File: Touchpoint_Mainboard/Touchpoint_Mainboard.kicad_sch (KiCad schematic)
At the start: 31 parts, among them J2 Conn_01x02, U4 NCP1117-3.3_SOT223, U5 W25Q128JVS, U6 RP2040, Y1 ABM8-272-T3

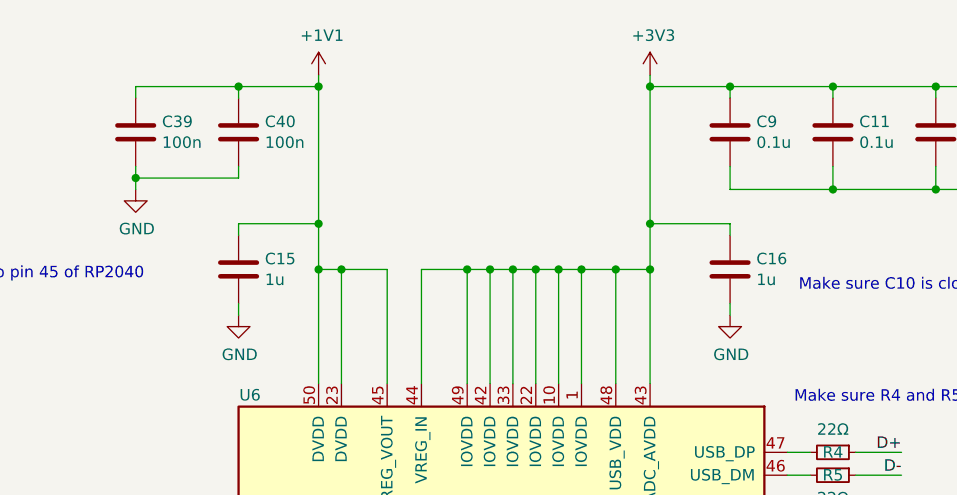
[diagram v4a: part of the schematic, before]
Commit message: Finished assigning footprints and 3d models for both boards
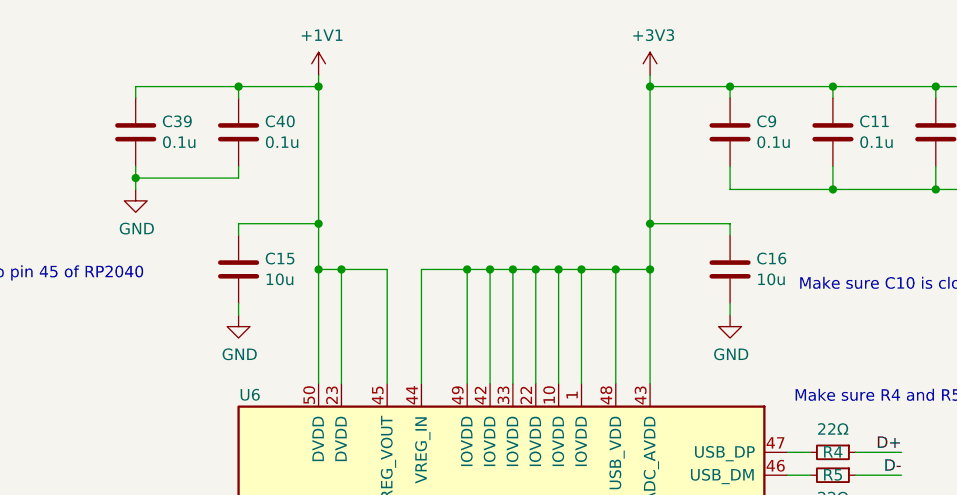
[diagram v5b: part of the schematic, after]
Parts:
- C15, C16: value 1u -> 10u
- C39, C40: value 100n -> 0.1u
- U5: footprint Package_SO:SOIC-8_5.23x5.23mm_P1.27mm -> Package_SO:SOIC-8_5.3x5.3mm_P1.27mm
- U6: footprint RP2040_minimal:RP2040-QFN-56 -> Package_DFN_QFN:QFN-56-1EP_7x7mm_P0.4mm_EP3.2x3.2mm
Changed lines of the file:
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@@
 			)
 		)
-		(property "Value" "1u"
+		(property "Value" "10u"
 			(at 38.481 45.593 0)
 			(effects
@@
 			)
 		)
-		(property "Value" "1u"
+		(property "Value" "10u"
 			(at 93.091 45.593 0)
 			(effects
@@
 			)
 		)
-		(property "Footprint" "Package_SO:SOIC-8_5.23x5.23mm_P1.27mm"
+		(property "Footprint" "Package_SO:SOIC-8_5.3x5.3mm_P1.27mm"
 			(at 229.87 121.92 0)
 			(effects
@@
 			)
 		)
-		(property "Footprint" "RP2040_minimal:RP2040-QFN-56"
+		(property "Footprint" "Package_DFN_QFN:QFN-56-1EP_7x7mm_P0.4mm_EP3.2x3.2mm"
 			(at 45.72 107.95 0)
 			(effects
@@
 			)
 		)
-		(property "Value" "100n"
+		(property "Value" "0.1u"
 			(at 38.481 30.353 0)
 			(effects
@@
 			)
 		)
-		(property "Value" "100n"
+		(property "Value" "0.1u"
 			(at 27.051 30.353 0)
 			(effects

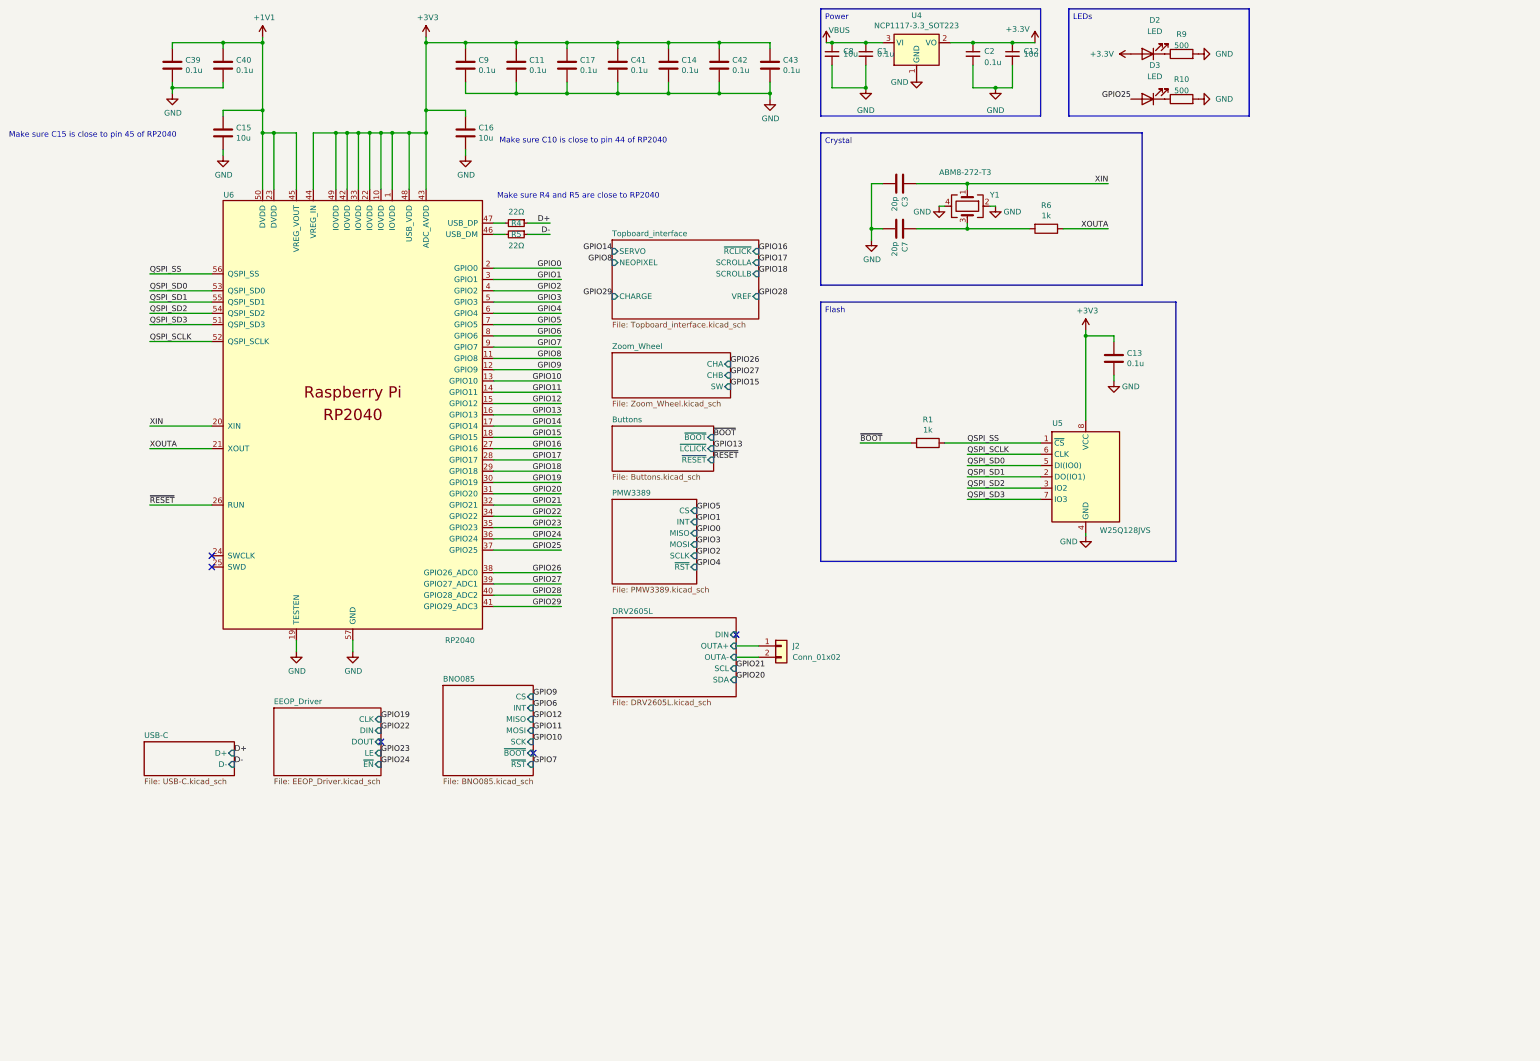
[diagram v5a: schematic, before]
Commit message: Added 3.3V to interface
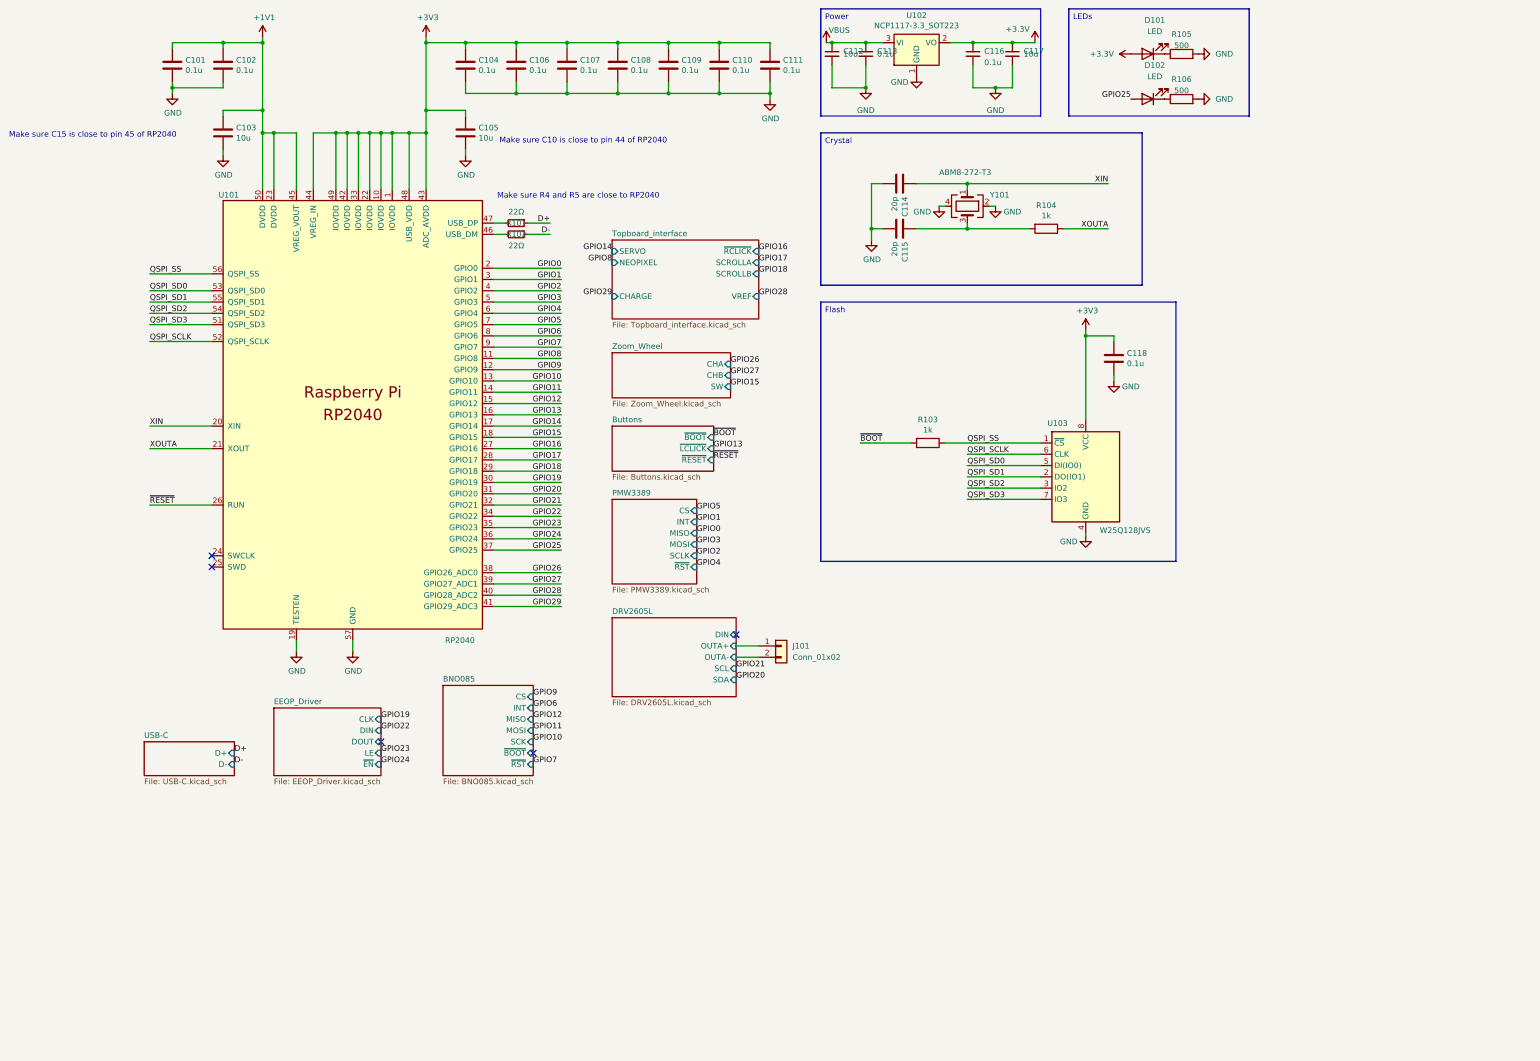
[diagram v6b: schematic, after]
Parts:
- renumbered C39 to C101, C40 to C102, C15 to C103, C9 to C104, C16 to C105, C11 to C106, C17 to C107, C41 to C108, C14 to C109, C42 to C110, C43 to C111, C8 to C112, C1 to C113, C3 to C114, C7 to C115, C2 to C116, C12 to C117, C13 to C118, D2 to D101, D3 to D102, J2 to J101, R4 to R101, R5 to R102, R1 to R103, R6 to R104, R9 to R105, R10 to R106, U6 to U101, U4 to U102, U5 to U103, Y1 to Y101

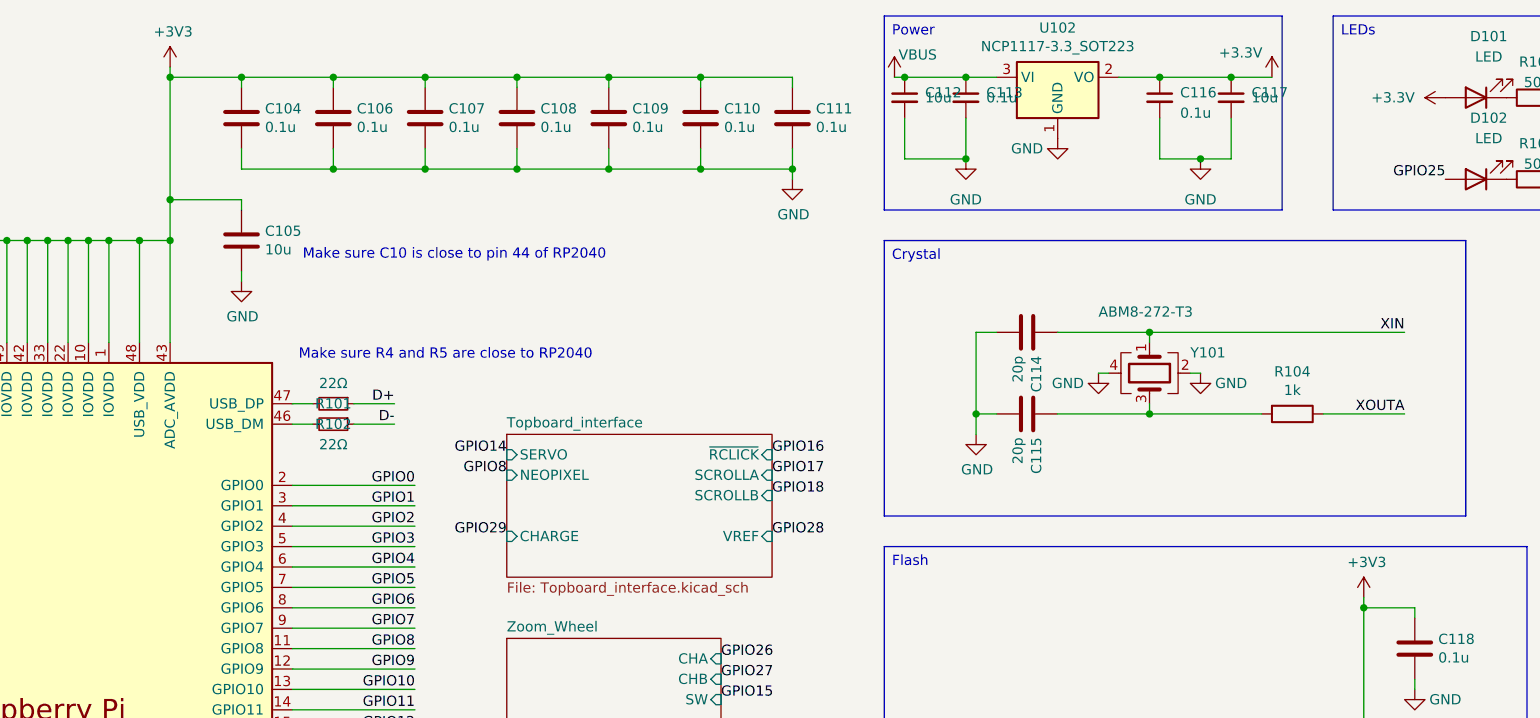
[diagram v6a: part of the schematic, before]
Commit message: Working through mainboard routing
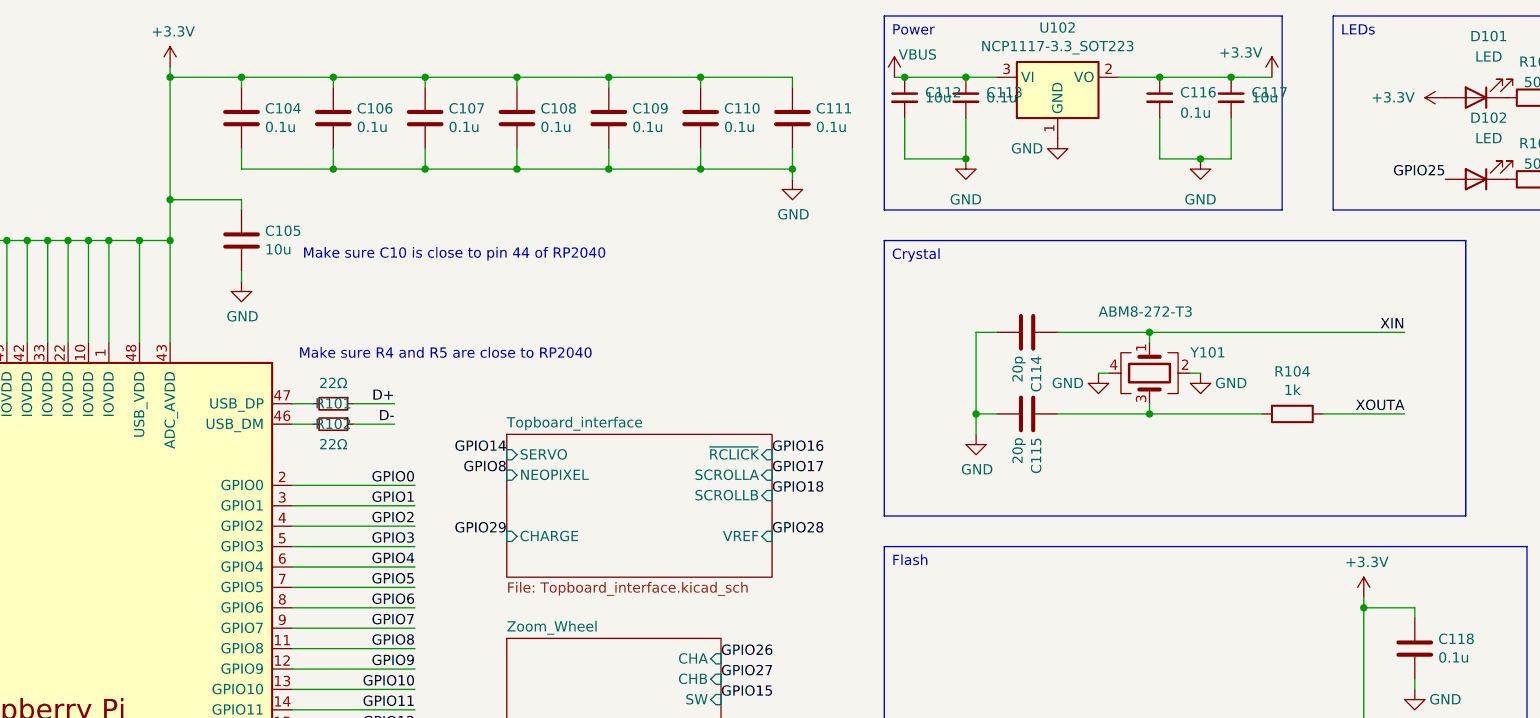
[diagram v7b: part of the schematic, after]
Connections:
- net +3V3 is gone; now on net +3.3V: C104.1, C105.1, C106.1, C107.1, C108.1, C109.1, C110.1, C111.1, C118.1, U101.1 (IOVDD), U101.10 (IOVDD), U101.22 (IOVDD), U101.33 (IOVDD), U101.42 (IOVDD), U101.43 (ADC_AVDD), U101.44 (VREG_IN), U101.48 (USB_VDD), U101.49 (IOVDD), U103.8 (VCC)
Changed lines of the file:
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@@
 			)
 		)
-		(property "Value" "+3V3"
+		(property "Value" "+3.3V"
 			(at 230.251 84.5058 0)
 			(effects
@@
 			)
 		)
-		(property "Value" "+3V3"
+		(property "Value" "+3.3V"
 			(at 81.661 18.4658 0)
 			(effects

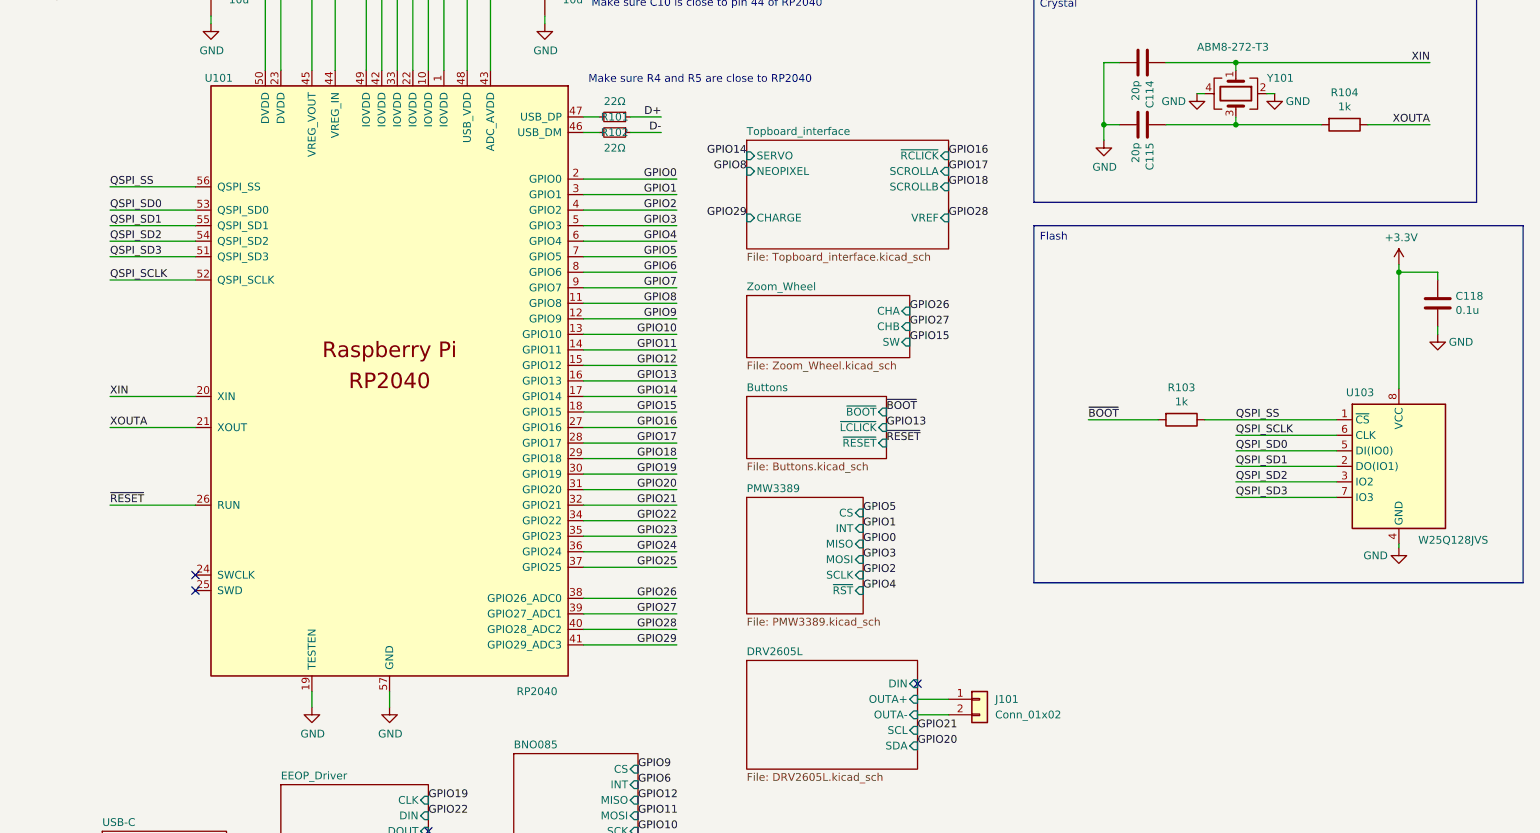
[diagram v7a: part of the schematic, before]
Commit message: Finally finished routing EEOP driver
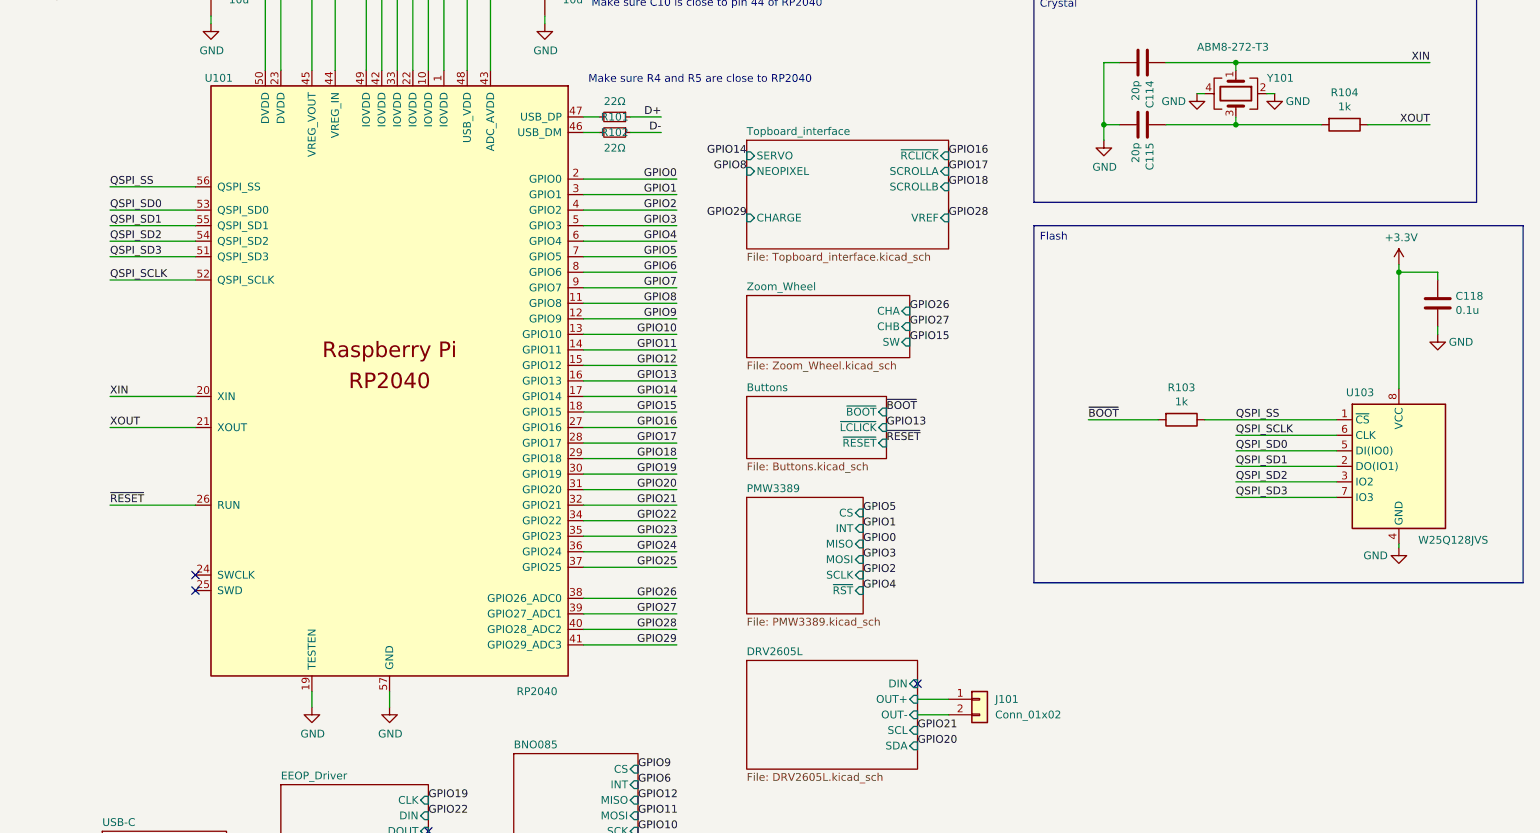
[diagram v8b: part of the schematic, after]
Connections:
- net DRV2605L/OUTA+ renamed DRV2605L/OUT+
- net DRV2605L/OUTA- renamed DRV2605L/OUT-
- net XOUTA renamed XOUT
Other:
- sheet DRV2605L ports: added OUT+, OUT-; removed OUTA+, OUTA-
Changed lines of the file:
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@@
 		)
 	)
-	(label "XOUTA"
+	(label "XOUT"
 		(at 234.95 66.04 180)
 		(effects
@@
 		)
 	)
-	(label "XOUTA"
+	(label "XOUT"
 		(at 19.05 115.57 0)
 		(effects
@@
 			)
 		)
-		(pin "OUTA+" input
+		(pin "OUT+" input
 			(at 151.13 160.02 0)
 			(effects
@@
 			)
 		)
-		(pin "OUTA-" input
+		(pin "OUT-" input
 			(at 151.13 162.56 0)
 			(effects
